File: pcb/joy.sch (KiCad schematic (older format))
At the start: 36 parts, among them J1 Conn_01x04, J2 Conn_01x05, U1 STM32F072CBTx, U2 TLV75533PDBV

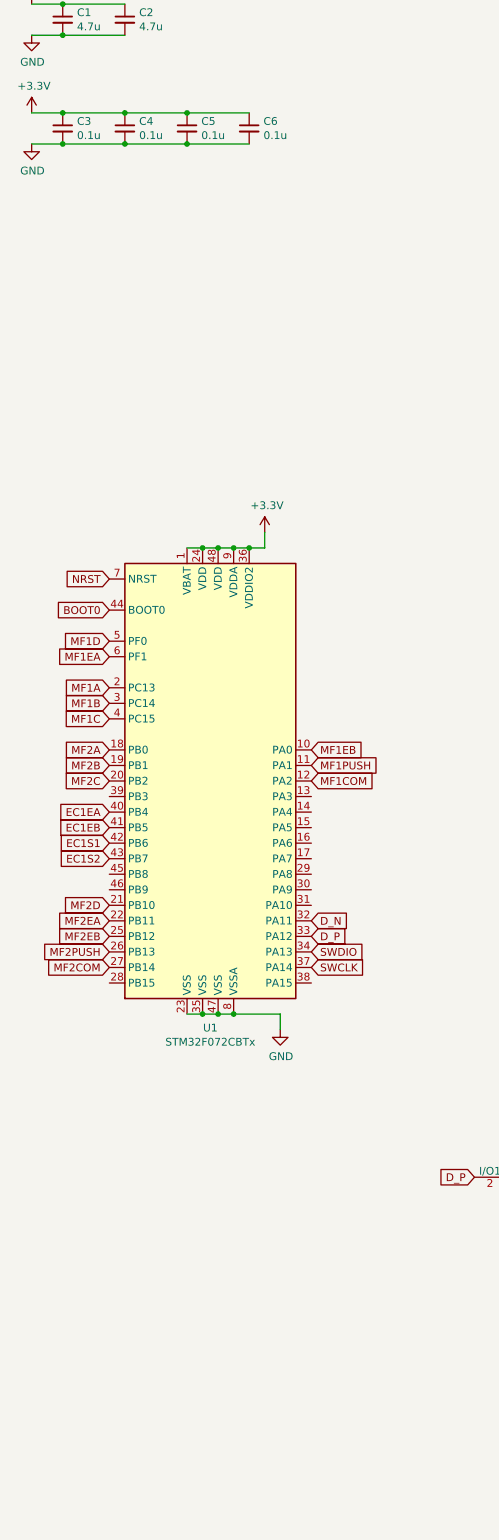
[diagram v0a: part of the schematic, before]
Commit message: added reset switches
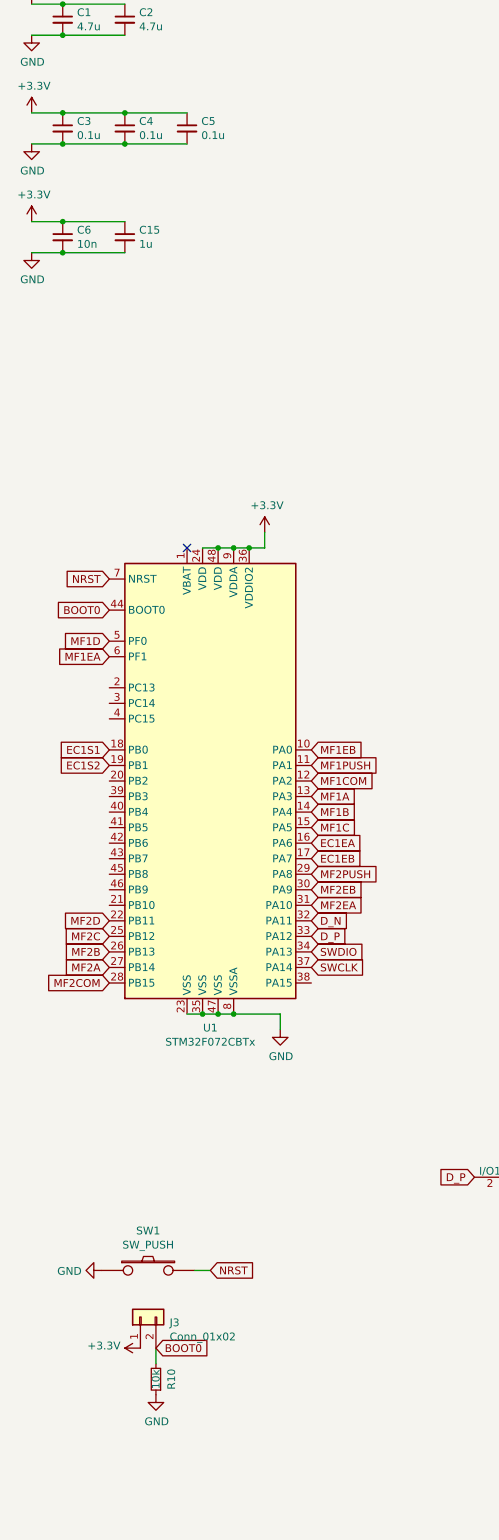
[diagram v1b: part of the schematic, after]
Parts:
- added C15: 1u, Capacitor_SMD:C_0603_1608Metric, symbol Device:C_Small
- added J3: Conn_01x02, Connector_PinHeader_2.54mm:PinHeader_1x02_P2.54mm_Vertical, symbol Connector_Generic:Conn_01x02
- added R10: 10k, Resistor_SMD:R_0603_1608Metric, symbol Device:R_Small
- added SW1: SW_PUSH, Button_Switch_SMD:SW_SPST_SKQG_WithStem, symbol keyboard_parts:SW_PUSH
- C6: value 0.1u -> 10n
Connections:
- net +3V3: now also C15.1, J3.1 (Pin_1); no longer U1.1 (VBAT)
- net BOOT0: now also J3.2 (Pin_2), R10.2
- net EC1EA: now also U1.16 (PA6); no longer U1.40 (PB4)
- net EC1EB: now also U1.17 (PA7); no longer U1.41 (PB5)
- net EC1S1: now also U1.18 (PB0); no longer U1.42 (PB6)
- net EC1S2: now also U1.19 (PB1); no longer U1.43 (PB7)
- net GND: now also C15.2, R10.1, SW1.1
- net MF1A: now also U1.13 (PA3); no longer U1.2 (PC13)
- net MF1B: now also U1.14 (PA4); no longer U1.3 (PC14)
- net MF1C: now also U1.15 (PA5); no longer U1.4 (PC15)
- net MF2A: now also U1.27 (PB14); no longer U1.18 (PB0)
- net MF2B: now also U1.26 (PB13); no longer U1.19 (PB1)
- net MF2C: now also U1.25 (PB12); no longer U1.20 (PB2)
- net MF2COM: now also U1.28 (PB15); no longer U1.27 (PB14)
- net MF2D: now also U1.22 (PB11); no longer U1.21 (PB10)
- net MF2EA: now also U1.31 (PA10); no longer U1.22 (PB11)
- net MF2EB: now also U1.30 (PA9); no longer U1.25 (PB12)
- net MF2PUSH: now also U1.29 (PA8); no longer U1.26 (PB13)
- net NRST: now also SW1.2
- no-connect marks 2 -> 3
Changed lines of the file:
@@
-$EndComp
-$Comp
-L Device:C_Small C6
-U 1 1 5D18333B
-P 2400 -250
-F 0 "C6" H 2492 -204 50  0000 L CNN
-F 1 "0.1u" H 2492 -295 50  0000 L CNN
-F 2 "Capacitor_SMD:C_0603_1608Metric" H 2400 -250 50  0001 C CNN
-F 3 "~" H 2400 -250 50  0001 C CNN
-	1    2400 -250
-	1    0    0    -1
 $EndComp
 $Comp
@@
 Wire Wire Line
 	1600 -350 2000 -350
-Connection ~ 2000 -350
-Wire Wire Line
-	2000 -350 2400 -350
-Wire Wire Line
-	2400 -150 2000 -150
 Connection ~ 1200 -150
 Wire Wire Line
@@
 Wire Wire Line
 	1600 -150 1200 -150
-Connection ~ 2000 -150
 Wire Wire Line
 	2000 -150 1600 -150
@@
 Wire Wire Line
 	2100 2450 2200 2450
-Wire Wire Line
-	2000 2450 2100 2450
-Connection ~ 2100 2450
 $Comp
 L MCU_ST_STM32F0:STM32F072CBTx U1
@@
 Text GLabel 10850 5900 2    50   Input ~ 0
 EC1S2
-Text GLabel 1500 3350 0    50   Input ~ 0
+Text GLabel 2800 4050 2    50   Input ~ 0
 MF1A
-Text GLabel 1500 3450 0    50   Input ~ 0
+Text GLabel 2800 4150 2    50   Input ~ 0
 MF1B
-Text GLabel 1500 3550 0    50   Input ~ 0
+Text GLabel 2800 4250 2    50   Input ~ 0
 MF1C
 Text GLabel 1500 3050 0    50   Input ~ 0
@@
 Text GLabel 2800 3950 2    50   Input ~ 0
 MF1COM
+Text GLabel 1500 5150 0    50   Input ~ 0
+MF2A
+Text GLabel 1500 5050 0    50   Input ~ 0
+MF2B
+Text GLabel 1500 4950 0    50   Input ~ 0
+MF2C
+Text GLabel 1500 4850 0    50   Input ~ 0
+MF2D
+Text GLabel 2800 4750 2    50   Input ~ 0
+MF2EA
+Text GLabel 2800 4650 2    50   Input ~ 0
+MF2EB
+Text GLabel 2800 4550 2    50   Input ~ 0
+MF2PUSH
+Text GLabel 1500 5250 0    50   Input ~ 0
+MF2COM
+Text GLabel 2800 4350 2    50   Input ~ 0
+EC1EA
+Text GLabel 2800 4450 2    50   Input ~ 0
+EC1EB
 Text GLabel 1500 3750 0    50   Input ~ 0
-MF2A
+EC1S1
 Text GLabel 1500 3850 0    50   Input ~ 0
-MF2B
-Text GLabel 1500 3950 0    50   Input ~ 0
-MF2C
-Text GLabel 1500 4750 0    50   Input ~ 0
-MF2D
-Text GLabel 1500 4850 0    50   Input ~ 0
-MF2EA
-Text GLabel 1500 4950 0    50   Input ~ 0
-MF2EB
-Text GLabel 1500 5050 0    50   Input ~ 0
-MF2PUSH
-Text GLabel 1500 5150 0    50   Input ~ 0
-MF2COM
-Text GLabel 1500 4150 0    50   Input ~ 0
-EC1EA
-Text GLabel 1500 4250 0    50   Input ~ 0
-EC1EB
-Text GLabel 1500 4350 0    50   Input ~ 0
-EC1S1
-Text GLabel 1500 4450 0    50   Input ~ 0
 EC1S2
 Text GLabel 5050 4550 3    50   Input ~ 0
@@
 	-1   0    0    1
 $EndComp
+$Comp
+L keyboard_parts:SW_PUSH SW1
+U 1 1 5D399C01
+P 1750 7100
+F 0 "SW1" H 1750 7355 50  0000 C CNN
+F 1 "SW_PUSH" H 1750 7264 50  0000 C CNN
+F 2 "Button_Switch_SMD:SW_SPST_SKQG_WithStem" H 1750 7100 60  0001 C CNN
+F 3 "" H 1750 7100 60  0000 C CNN
+	1    1750 7100
+	1    0    0    -1
+$EndComp
+Text GLabel 2150 7100 2    50   Input ~ 0
+NRST
+$Comp
+L power:GND #PWR037
+U 1 1 5D39BA71
+P 1450 7100
+F 0 "#PWR037" H 1450 6850 50  0001 C CNN
+F 1 "GND" V 1455 6972 50  0000 R CNN
+F 2 "" H 1450 7100 50  0001 C CNN
+F 3 "" H 1450 7100 50  0001 C CNN
+	1    1450 7100
+	0    1    1    0
+$EndComp
+Wire Wire Line
+	2050 7100 2150 7100
+$Comp
+L power:+3.3V #PWR038
+U 1 1 5D3A132B
+P 1700 7600
+F 0 "#PWR038" H 1700 7450 50  0001 C CNN
+F 1 "+3.3V" V 1715 7728 50  0000 L CNN
+F 2 "" H 1700 7600 50  0001 C CNN
+F 3 "" H 1700 7600 50  0001 C CNN
+	1    1700 7600
+	0    -1   -1   0
+$EndComp
+$Comp
+L Device:R_Small R10
+U 1 1 5D3A402B
+P 1800 7800
+F 0 "R10" V 1700 7800 50  0000 C CNN
+F 1 "10k" V 1800 7800 50  0000 C CNN
+F 2 "Resistor_SMD:R_0603_1608Metric" H 1800 7800 50  0001 C CNN
+F 3 "~" H 1800 7800 50  0001 C CNN
+	1    1800 7800
+	-1   0    0    1
+$EndComp
+$Comp
+L power:GND #PWR039
+U 1 1 5D3A49AD
+P 1800 7900
+F 0 "#PWR039" H 1800 7650 50  0001 C CNN
+F 1 "GND" H 1805 7727 50  0000 C CNN
+F 2 "" H 1800 7900 50  0001 C CNN
+F 3 "" H 1800 7900 50  0001 C CNN
+	1    1800 7900
+	1    0    0    -1
+$EndComp
+Text GLabel 1800 7600 2    50   Input ~ 0
+BOOT0
+$Comp
+L Connector_Generic:Conn_01x02 J3
+U 1 1 5D3AA815
+P 1700 7400
+F 0 "J3" V 1664 7212 50  0000 R CNN
+F 1 "Conn_01x02" V 1573 7212 50  0000 R CNN
+F 2 "Connector_PinHeader_2.54mm:PinHeader_1x02_P2.54mm_Vertical" H 1700 7400 50  0001 C CNN
+F 3 "~" H 1700 7400 50  0001 C CNN
+	1    1700 7400
+	0    -1   -1   0
+$EndComp
+Wire Wire Line
+	1800 7600 1800 7700
+NoConn ~ 2000 2450
+$Comp
+L Device:C_Small C6
+U 1 1 5D3D64FF
+P 1200 450
+F 0 "C6" H 1292 496 50  0000 L CNN
+F 1 "10n" H 1292 405 50  0000 L CNN
+F 2 "Capacitor_SMD:C_0603_1608Metric" H 1200 450 50  0001 C CNN
+F 3 "~" H 1200 450 50  0001 C CNN
+	1    1200 450
+	1    0    0    -1
+$EndComp
+$Comp
+L Device:C_Small C15
+U 1 1 5D3D6505
+P 1600 450
+F 0 "C15" H 1692 496 50  0000 L CNN
+F 1 "1u" H 1692 405 50  0000 L CNN
+F 2 "Capacitor_SMD:C_0603_1608Metric" H 1600 450 50  0001 C CNN
+F 3 "~" H 1600 450 50  0001 C CNN
+	1    1600 450
+	1    0    0    -1
+$EndComp
+$Comp
+L power:GND #PWR040
+U 1 1 5D3D650B
+P 1000 550
+F 0 "#PWR040" H 1000 300 50  0001 C CNN
+F 1 "GND" H 1005 377 50  0000 C CNN
+F 2 "" H 1000 550 50  0001 C CNN
+F 3 "" H 1000 550 50  0001 C CNN
+	1    1000 550
+	1    0    0    -1
+$EndComp
+$Comp
+L power:+3.3V #PWR036
+U 1 1 5D3D6511
+P 1000 350
+F 0 "#PWR036" H 1000 200 50  0001 C CNN
+F 1 "+3.3V" H 1015 523 50  0000 C CNN
+F 2 "" H 1000 350 50  0001 C CNN
+F 3 "" H 1000 350 50  0001 C CNN
+	1    1000 350
+	1    0    0    -1
+$EndComp
+Wire Wire Line
+	1000 350  1200 350
+Connection ~ 1200 350
+Wire Wire Line
+	1200 350  1600 350
+Connection ~ 1200 550
+Wire Wire Line
+	1200 550  1000 550
+Wire Wire Line
+	1600 550  1200 550
 $EndSCHEMATC

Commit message: added switches, redid routing, updated pins
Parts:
- removed J3: Conn_01x02, Connector_PinHeader_2.54mm:PinHeader_1x02_P2.54mm_Vertical, symbol Connector_Generic:Conn_01x02
- added SW2: SW_PUSH, Button_Switch_SMD:SW_SPST_SKQG_WithStem, symbol keyboard_parts:SW_PUSH
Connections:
- net +3V3: now also SW2.1
- net BOOT0: now also SW2.2
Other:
- moved on the sheet: R10
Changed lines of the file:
@@
 EESchema Schematic File Version 4
+LIBS:joy-cache
 EELAYER 29 0
 EELAYER END
@@
 L power:+3.3V #PWR038
 U 1 1 5D3A132B
-P 1700 7600
-F 0 "#PWR038" H 1700 7450 50  0001 C CNN
-F 1 "+3.3V" V 1715 7728 50  0000 L CNN
-F 2 "" H 1700 7600 50  0001 C CNN
-F 3 "" H 1700 7600 50  0001 C CNN
-	1    1700 7600
+P 1450 7450
+F 0 "#PWR038" H 1450 7300 50  0001 C CNN
+F 1 "+3.3V" V 1465 7578 50  0000 L CNN
+F 2 "" H 1450 7450 50  0001 C CNN
+F 3 "" H 1450 7450 50  0001 C CNN
+	1    1450 7450
 	0    -1   -1   0
 $EndComp
@@
 L Device:R_Small R10
 U 1 1 5D3A402B
-P 1800 7800
-F 0 "R10" V 1700 7800 50  0000 C CNN
-F 1 "10k" V 1800 7800 50  0000 C CNN
-F 2 "Resistor_SMD:R_0603_1608Metric" H 1800 7800 50  0001 C CNN
-F 3 "~" H 1800 7800 50  0001 C CNN
-	1    1800 7800
+P 2050 7650
+F 0 "R10" V 1950 7650 50  0000 C CNN
+F 1 "10k" V 2050 7650 50  0000 C CNN
+F 2 "Resistor_SMD:R_0603_1608Metric" H 2050 7650 50  0001 C CNN
+F 3 "~" H 2050 7650 50  0001 C CNN
+	1    2050 7650
 	-1   0    0    1
 $EndComp
@@
 L power:GND #PWR039
 U 1 1 5D3A49AD
-P 1800 7900
-F 0 "#PWR039" H 1800 7650 50  0001 C CNN
-F 1 "GND" H 1805 7727 50  0000 C CNN
-F 2 "" H 1800 7900 50  0001 C CNN
-F 3 "" H 1800 7900 50  0001 C CNN
-	1    1800 7900
-	1    0    0    -1
-$EndComp
-Text GLabel 1800 7600 2    50   Input ~ 0
+P 2050 7750
+F 0 "#PWR039" H 2050 7500 50  0001 C CNN
+F 1 "GND" H 2055 7577 50  0000 C CNN
+F 2 "" H 2050 7750 50  0001 C CNN
+F 3 "" H 2050 7750 50  0001 C CNN
+	1    2050 7750
+	1    0    0    -1
+$EndComp
+Text GLabel 2050 7450 2    50   Input ~ 0
 BOOT0
-$Comp
-L Connector_Generic:Conn_01x02 J3
-U 1 1 5D3AA815
-P 1700 7400
-F 0 "J3" V 1664 7212 50  0000 R CNN
-F 1 "Conn_01x02" V 1573 7212 50  0000 R CNN
-F 2 "Connector_PinHeader_2.54mm:PinHeader_1x02_P2.54mm_Vertical" H 1700 7400 50  0001 C CNN
-F 3 "~" H 1700 7400 50  0001 C CNN
-	1    1700 7400
-	0    -1   -1   0
-$EndComp
-Wire Wire Line
-	1800 7600 1800 7700
+Wire Wire Line
+	2050 7450 2050 7550
 NoConn ~ 2000 2450
 $Comp
@@
 Wire Wire Line
 	1600 550  1200 550
+$Comp
+L keyboard_parts:SW_PUSH SW2
+U 1 1 5D18B7EF
+P 1750 7450
+F 0 "SW2" H 1750 7705 50  0000 C CNN
+F 1 "SW_PUSH" H 1750 7614 50  0000 C CNN
+F 2 "Button_Switch_SMD:SW_SPST_SKQG_WithStem" H 1750 7450 60  0001 C CNN
+F 3 "" H 1750 7450 60  0000 C CNN
+	1    1750 7450
+	1    0    0    -1
+$EndComp
 $EndSCHEMATC

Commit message: beautified schem
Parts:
- MF1, MF2: symbol crokto:Alps_RKJXx -> joy-rescue:Alps_RKJXx-crokto
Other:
- moved on the sheet: C1, C10, C11, C12, C13, C14, C15, C2, C3, C4, C5, C6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
